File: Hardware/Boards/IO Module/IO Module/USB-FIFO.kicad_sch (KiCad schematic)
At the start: 0 parts

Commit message: Updated IO Module Schematics
Added Power, USB hub and USB-JTAG circuits
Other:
- company: (none) -> Drexel University
- title: (none) -> USB-FIFO
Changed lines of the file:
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@@
 	(generator "eeschema")
 	(generator_version "8.0")
-	(paper "A4")
+	(paper "A3")
+	(title_block
+		(title "USB-FIFO")
+		(date "2024-07-14")
+		(rev "1.0")
+		(company "Drexel University")
+		(comment 1 "Designed by John Hofmeyr")
+	)
 )

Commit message: Updated IO Module Schematics
Added MCU, JTAG and FIFO circuits
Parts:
- added C82, C83: 18pF, Capacitor_SMD:C_0402_1005Metric, symbol Device:C_Small
- added C84, C86, C87, C88, C90, C91, C92, C93, C94, C95, C97, C98, C99: 100nF, Capacitor_SMD:C_0402_1005Metric, symbol Device:C_Small
- added C85, C96: 1uF, Capacitor_SMD:C_0402_1005Metric, symbol Device:C_Small
- added C89: 10uF, Capacitor_SMD:C_0603_1608Metric, symbol Device:C_Small
- added R61, R62, R63: 10K, Resistor_SMD:R_0402_1005Metric, symbol Device:R_US
- added R64: 5.1K, Resistor_SMD:R_0402_1005Metric, symbol Device:R_US
- added R65: 1K, Resistor_SMD:R_0402_1005Metric, symbol Device:R_US
- added U16: FT600Q, Package_DFN_QFN:QFN-56-1EP_7x7mm_P0.4mm_EP4x4mm, symbol IO_Module:FT600Q
- added Y3: 30Mhz, Oscillator:Oscillator_SMD_Abracon_ASE-4Pin_3.2x2.5mm, symbol Device:Crystal_GND24_Small
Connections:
- new net +3V3: C84.1, C85.1, C86.1, C87.1, C88.1, C96.1, C97.1, C98.1, C99.1, R61.2, R62.2, R63.2, U16.15 (VCC33), U16.19 (VCC33), U16.22 (VDDA), U16.30 (VCC33), U16.38 (VCCIO), U16.44 (VCCIO), U16.52 (VCCIO)
- new net FIFO_BE0: U16.2 (BE_0)
- new net FIFO_BE1: U16.3 (BE_1)
- new net FIFO_CLK: U16.43 (CLK)
- new net FIFO_D0: U16.33 (D0)
- new net FIFO_D1: U16.34 (D1)
- new net FIFO_D10: U16.47 (D10)
- new net FIFO_D11: U16.48 (D11)
- new net FIFO_D12: U16.53 (D12)
- new net FIFO_D13: U16.54 (D13)
- new net FIFO_D14: U16.55 (D14)
- new net FIFO_D15: U16.56 (D15)
- new net FIFO_D2: U16.35 (D2)
- new net FIFO_D3: U16.36 (D3)
- new net FIFO_D4: U16.39 (D4)
- new net FIFO_D5: U16.40 (D5)
- new net FIFO_D6: U16.41 (D6)
- new net FIFO_D7: U16.42 (D7)
- new net FIFO_D8: U16.45 (D8)
- new net FIFO_D9: U16.46 (D9)
- new net FT600_OE: U16.9 (OE_N)
- new net FT600_RD: U16.8 (RD_N)
- new net FT600_RST: R62.1, U16.10 (RST_N)
- new net FT600_RXE: U16.5 (RXF_N)
- new net FT600_SIWU: R63.1, U16.6 (SIWU_N)
- new net FT600_TXE: U16.4 (TXE_N)
- new net FT600_VCORE: C89.1, C90.1, C91.1, C92.1, C93.1, C94.1, C95.1, U16.1 (AVDD), U16.23 (VD10), U16.26 (VD10), U16.31 (VD10), U16.37 (VD10), U16.50 (VD10)
- new net FT600_VUSB: R64.1, R65.2, U16.29 (VBUS)
- new net FT600_WAKEUP: R61.1, U16.11 (WAKEUP_N)
- new net FT600_WR: U16.7 (WR_N)
- new net FT600_XI: C82.1, U16.16 (XI), Y3.1
- new net FT600_XO: C83.1, U16.17 (XO), Y3.3
- new net GND: C82.2, C83.2, C84.2, C85.2, C86.2, C87.2, C88.2, C89.2, C90.2, C91.2, C92.2, C93.2, C94.2, C95.2, C96.2, C97.2, C98.2, C99.2, R65.1, U16.32 (GND), U16.49 (GND), U16.51 (GND), U16.57 (EPAD), Y3.2, Y3.4
- new net PP_VUSB: R64.2
- new net USB_FIFO_D_N: U16.20 (DN)
- new net USB_FIFO_D_P: U16.18 (DP)
- new net USB_FIFO_RX_N: U16.27 (RIDN)
- new net USB_FIFO_RX_P: U16.28 (RIDP)
- new net USB_FIFO_TX_N: U16.24 (TODN)
- new net USB_FIFO_TX_P: U16.25 (TODP)
- no-connect marks 0 -> 3

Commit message: Completed IO Module Schematics
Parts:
- renumbered C89 to C49, C90 to C50, C91 to C51, C92 to C52, C93 to C53, C94 to C54, C95 to C55, C99 to C56, C98 to C57, C97 to C58, C96 to C59, C85 to C60, C84 to C61, C86 to C62, C87 to C63, C88 to C64, C82 to C65, C83 to C66, R64 to R42, R63 to R43, R62 to R44, R65 to R45, R61 to R46, U16 to U13, Y3 to Y2

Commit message: PCB Layout Started
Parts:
- added R103: 1.6K, Resistor_SMD:R_0402_1005Metric, symbol Device:R_US
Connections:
- net GND: now also R103.2
- new net: R103.1, U13.21 (RREF)
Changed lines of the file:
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@@
 	(wire
 		(pts
+			(xy 179.07 157.48) (xy 179.07 161.29)
+		)
+		(stroke
+			(width 0)
+			(type default)
+		)
+	)
+	(wire
+		(pts
 			(xy 176.53 129.54) (xy 193.04 129.54)
 		)
@@
 	(wire
 		(pts
+			(xy 189.23 157.48) (xy 193.04 157.48)
+		)
+		(stroke
+			(width 0)
+			(type default)
+		)
+	)
+	(wire
+		(pts
 			(xy 156.21 69.85) (xy 167.64 69.85)
 		)
@@
 	(wire
 		(pts
+			(xy 181.61 157.48) (xy 179.07 157.48)
+		)
+		(stroke
+			(width 0)
+			(type default)
+		)
+	)
+	(wire
+		(pts
 			(xy 165.1 105.41) (xy 165.1 104.14)
 		)
@@
 		(pin "51"
 		)
+		(pin "21"
+		)
 		(instances
 			(project ""
@@
 	(symbol
 		(lib_id "power:GND")
+		(at 179.07 161.29 0)
+		(unit 1)
+		(exclude_from_sim no)
+		(in_bom yes)
+		(on_board yes)
+		(dnp no)
+		(property "Reference" "#PWR0273"
+			(at 179.07 165.1 0)
+			(effects
+				(font
+					(size 1.27 1.27)
+				)
+				(hide yes)
+			)
+		)
+		(property "Value" "GND"
+			(at 179.07 165.1 0)
+			(effects
+				(font
+					(size 1.27 1.27)
+				)
+			)
+		)
+		(property "Footprint" ""
+			(at 179.07 161.29 0)
+			(effects
+				(font
+					(size 1.27 1.27)
+				)
+				(hide yes)
+			)
+		)
+		(property "Datasheet" ""
+			(at 179.07 161.29 0)
+			(effects
+				(font
+					(size 1.27 1.27)
+				)
+				(hide yes)
+			)
+		)
+		(property "Description" "Power symbol creates a global label with name \"GND\" , ground"
+			(at 179.07 161.29 0)
+			(effects
+				(font
+					(size 1.27 1.27)
+				)
+				(hide yes)
+			)
+		)
+		(pin "1"
+		)
+		(instances
+			(project "IO Module"
+				(path "/884396b6-238b-495e-b731-e47ad2523f76/dcc99803-8acd-4632-9c0b-7f677477cf65/0caf3050-48d7-4c2b-bd75-8084d37ef6b3"
+					(reference "#PWR0273")
+					(unit 1)
+				)
+			)
+		)
+	)
+	(symbol
+		(lib_id "power:GND")
 		(at 176.53 111.76 0)
 		(unit 1)
@@
 					(unit 1)
 				)
+			)
+		)
+	)
+	(symbol
+		(lib_id "Device:R_US")
+		(at 185.42 157.48 270)
+		(unit 1)
+		(exclude_from_sim no)
+		(in_bom yes)
+		(on_board yes)
+		(dnp no)
+		(fields_autoplaced yes)
+		(property "Reference" "R103"
+			(at 185.42 151.13 90)
+			(effects
+				(font
+					(size 1.27 1.27)
+				)
+			)
+		)
+		(property "Value" "1.6K"
+			(at 185.42 153.67 90)
+			(effects
+				(font
+					(size 1.27 1.27)
+				)
+			)
+		)
+		(property "Footprint" "Resistor_SMD:R_0402_1005Metric"
+			(at 185.166 158.496 90)
+			(effects
+				(font
+					(size 1.27 1.27)
+				)
+				(hide yes)
+			)
+		)
+		(property "Datasheet" "~"
+			(at 185.42 157.48 0)
+			(effects
+				(font
+					(size 1.27 1.27)
+				)
+				(hide yes)
+			)
+		)
+		(property "Description" "Resistor, US symbol"
+			(at 185.42 157.48 0)
+			(effects
+				(font
+					(size 1.27 1.27)
+				)
+				(hide yes)
+			)
+		)
+		(pin "2"
+		)
+		(pin "1"
+		)
+		(instances
+			(project "IO Module"
+				(path "/884396b6-238b-495e-b731-e47ad2523f76/dcc99803-8acd-4632-9c0b-7f677477cf65/0caf3050-48d7-4c2b-bd75-8084d37ef6b3"
+					(reference "R103")
+					(unit 1)
+				)

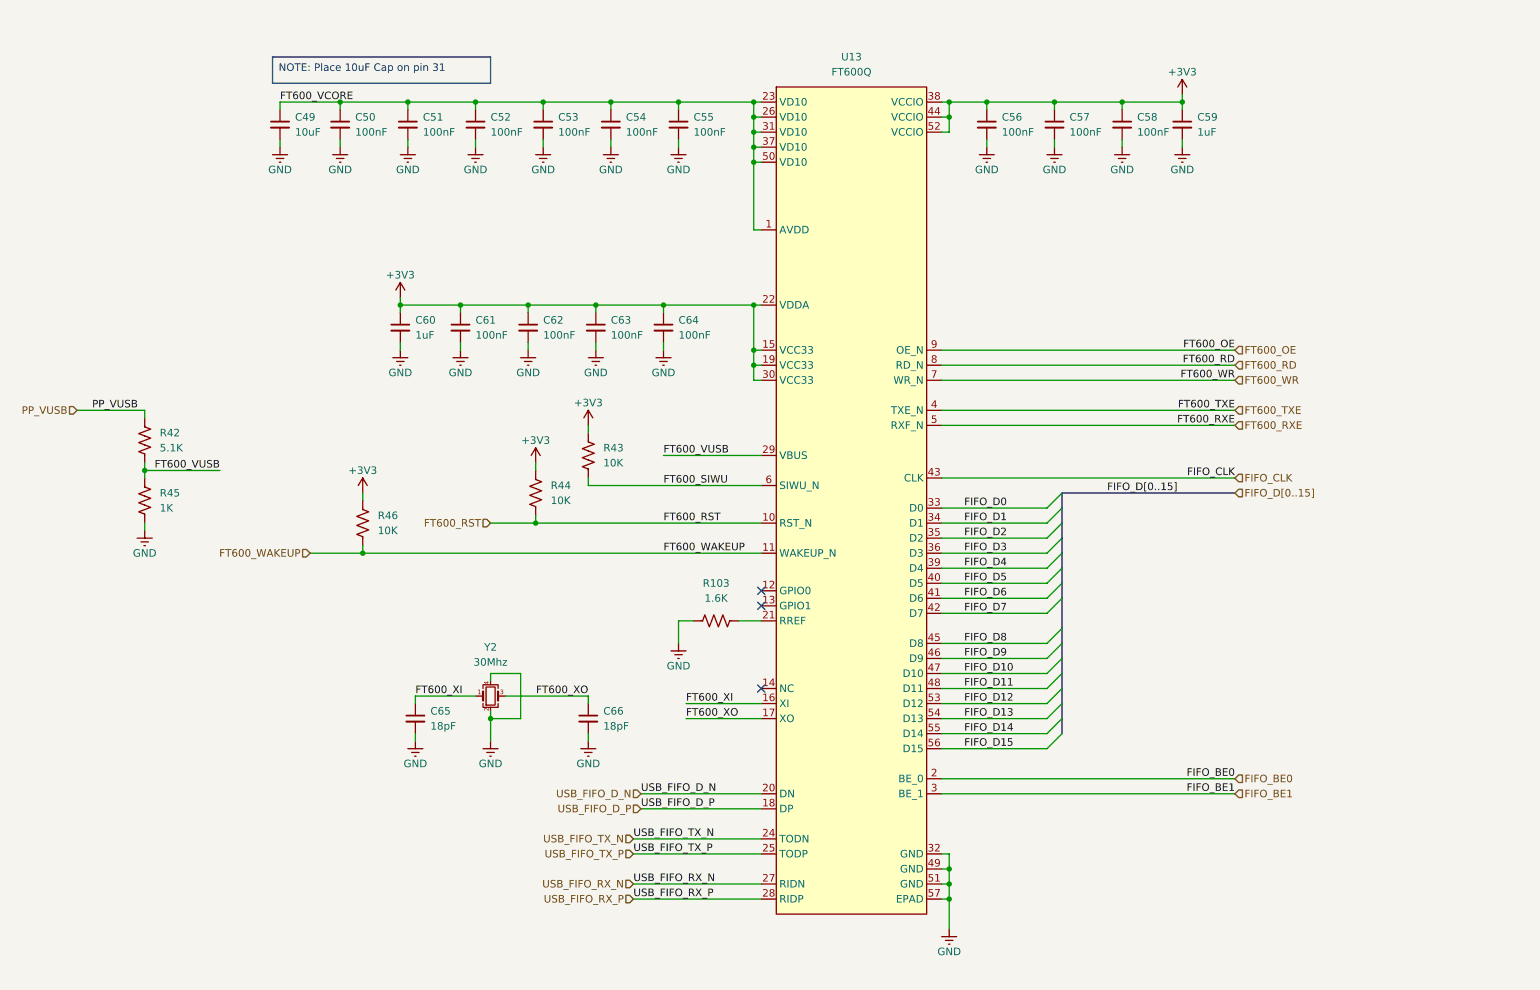
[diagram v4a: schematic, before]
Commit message: Updated SCH with notes & annotations
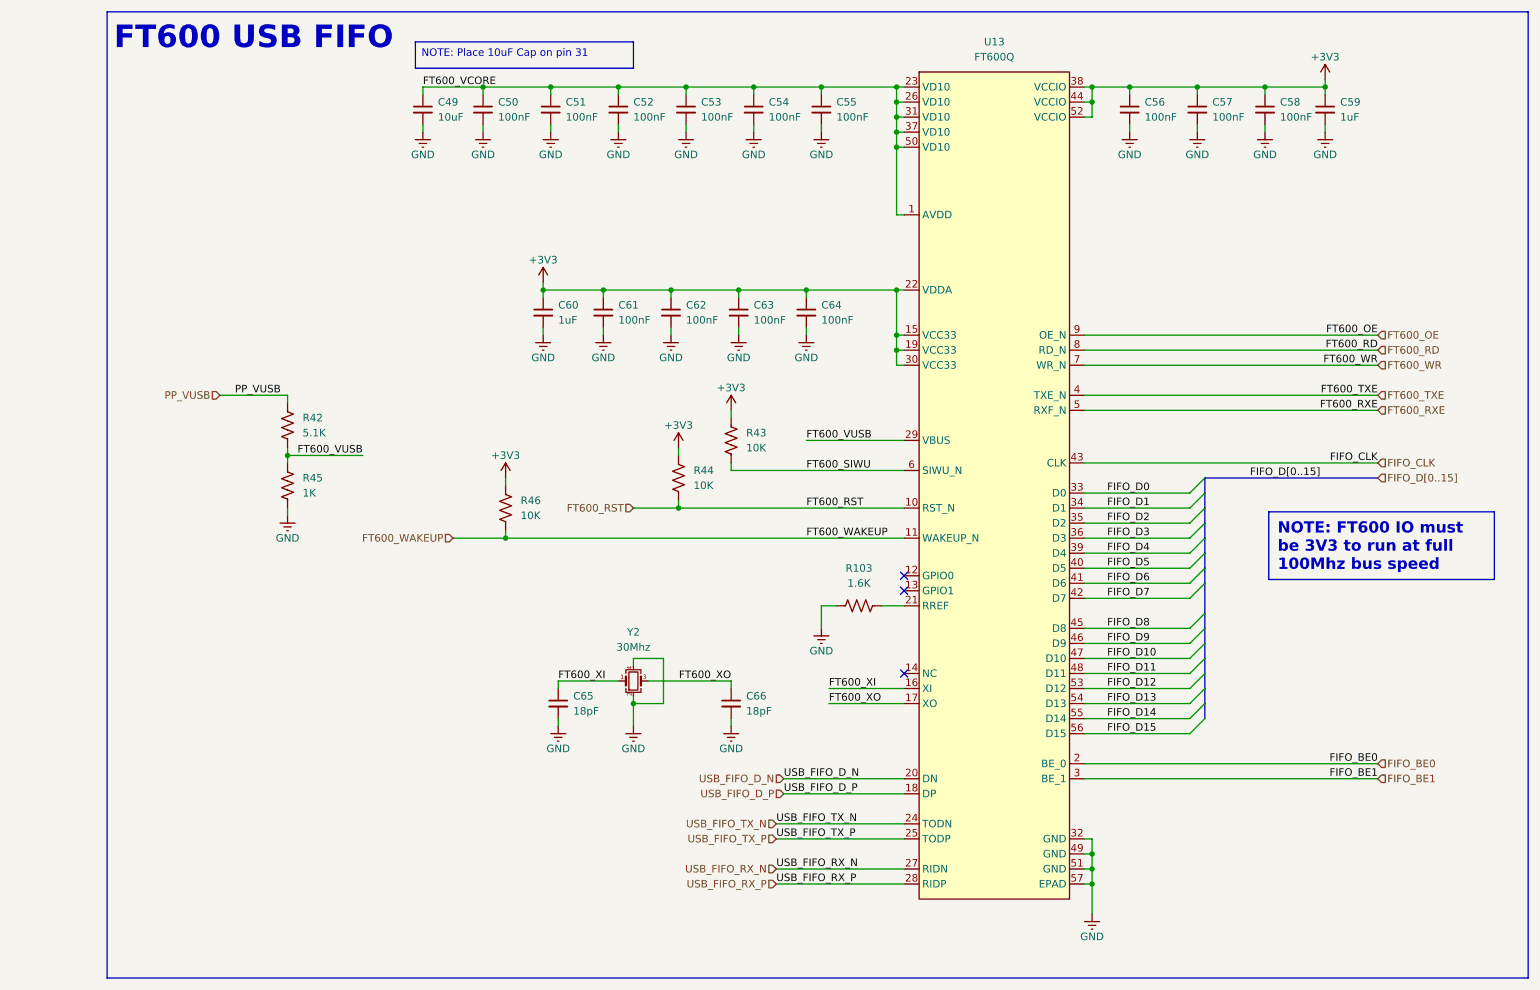
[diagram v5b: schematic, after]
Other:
- note added: "FT600 USB FIFO"
- moved on the sheet: C49, C50, C51, C52, C53, C54, C55, C56, C57, C58, C59, C60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
